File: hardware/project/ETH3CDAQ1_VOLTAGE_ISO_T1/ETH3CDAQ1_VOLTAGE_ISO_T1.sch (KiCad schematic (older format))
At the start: 86 parts, among them J1 GMSTB2,5/2-GF-7,62, J2 Conn_02x10_Odd_Even, U1 DG211, U10 74LVC1GU04DRL, U11 74LVC1GU04DRL, U12 TXB0104PW, U13 24LC08B-E/MS, U14 LT3032-15, U15 PCA9557PW, U2 DG419DY, U3 LT3032, U4 OPA140, U5 ISO124, U6 ADuM5410, U7 DCP020515DU, U8 OPA237_SOT23, U9 74LVC1GU04DRL

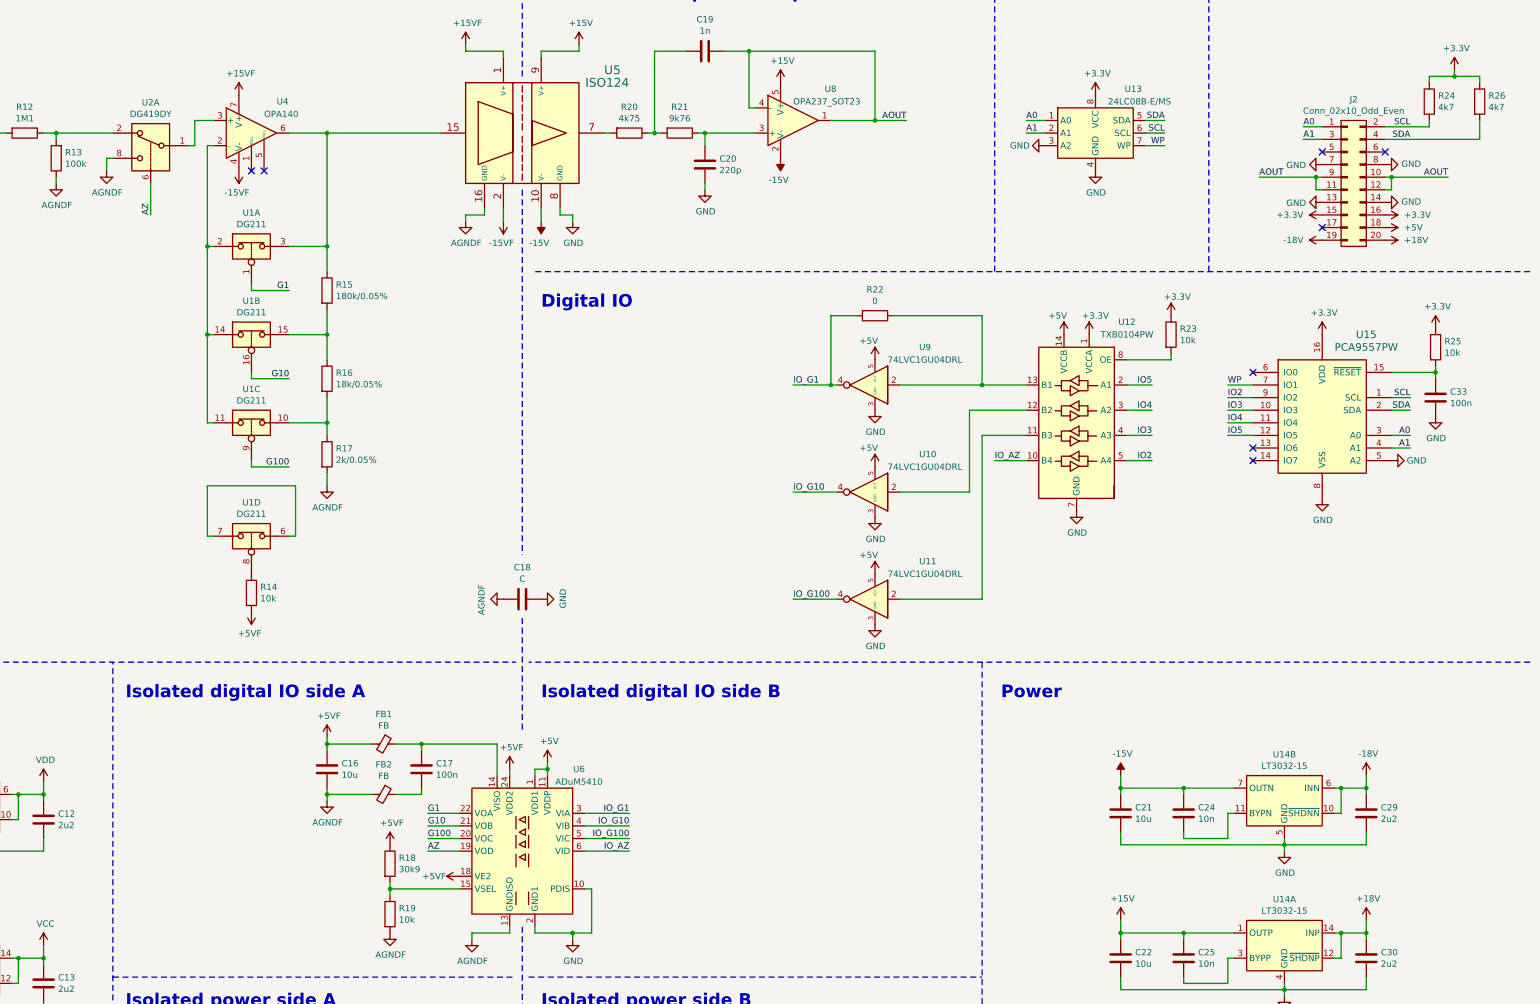
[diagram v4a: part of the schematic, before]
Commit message: Added SDRAM to the linker file.
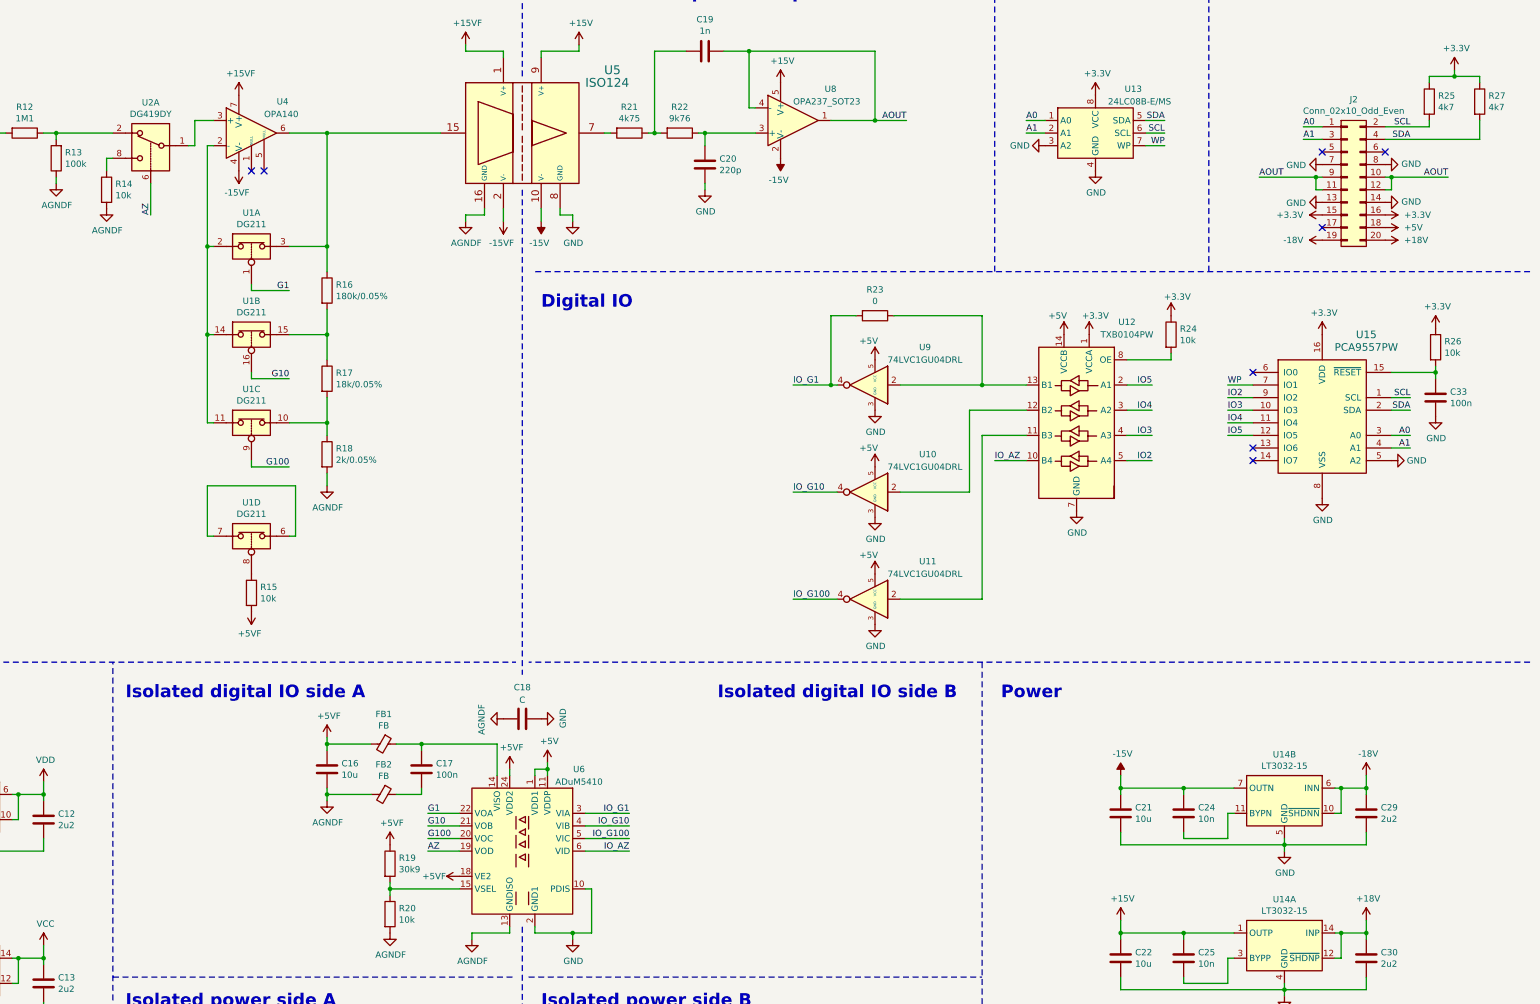
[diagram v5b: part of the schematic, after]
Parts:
- added R14: 10k, Resistor_SMD:R_0603_1608Metric_Pad0.98x0.95mm_HandSolder, symbol Device:R
- renumbered R14 to R15, R15 to R16, R16 to R17, R17 to R18, R18 to R19, R19 to R20, R20 to R21, R21 to R22, R22 to R23, R23 to R24, R24 to R25, R25 to R26, R26 to R27
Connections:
- net AGNDF: now also R14.2; no longer U2.8
- new net: R14.1, U2.8
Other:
- moved on the sheet: C18
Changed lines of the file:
@@
 	5550 2700 5600 2700
 $Comp
-L Device:R R15
+L Device:R R16
 U 1 1 5FCA8528
 P 6500 3050
-F 0 "R15" H 6570 3096 50  0000 L CNN
+F 0 "R16" H 6570 3096 50  0000 L CNN
 F 1 "180k/0.05%" H 6570 3005 50  0000 L CNN
 F 2 "Resistor_SMD:R_0603_1608Metric_Pad0.98x0.95mm_HandSolder" V 6430 3050 50  0001 C CNN
@@
 	5550 3400 5550 2700
 $Comp
-L Device:R R16
+L Device:R R17
 U 1 1 5FCC997F
 P 6500 3750
-F 0 "R16" H 6570 3796 50  0000 L CNN
+F 0 "R17" H 6570 3796 50  0000 L CNN
 F 1 "18k/0.05%" H 6570 3705 50  0000 L CNN
 F 2 "Resistor_SMD:R_0603_1608Metric_Pad0.98x0.95mm_HandSolder" V 6430 3750 50  0001 C CNN
@@
 Connection ~ 5550 3400
 $Comp
-L Device:R R17
+L Device:R R18
 U 1 1 5FCD9876
 P 6500 4350
-F 0 "R17" H 6570 4396 50  0000 L CNN
+F 0 "R18" H 6570 4396 50  0000 L CNN
 F 1 "2k/0.05%" H 6570 4305 50  0000 L CNN
 F 2 "Resistor_SMD:R_0603_1608Metric_Pad0.98x0.95mm_HandSolder" V 6430 4350 50  0001 C CNN
@@
 $EndComp
 $Comp
-L Device:R R14
+L Device:R R15
 U 1 1 5FCE80CD
 P 5900 5450
-F 0 "R14" H 5970 5496 50  0000 L CNN
+F 0 "R15" H 5970 5496 50  0000 L CNN
 F 1 "10k" H 5970 5405 50  0000 L CNN
 F 2 "Resistor_SMD:R_0603_1608Metric_Pad0.98x0.95mm_HandSolder" V 5830 5450 50  0001 C CNN
@@
 L ETH3CDAQ1:AGNDF #PWR028
 U 1 1 5FCEDC4F
-P 4750 2100
-F 0 "#PWR028" H 4750 1850 50  0001 C CNN
-F 1 "AGNDF" H 4755 1927 50  0000 C CNN
-F 2 "" H 4750 2100 50  0001 C CNN
-F 3 "" H 4750 2100 50  0001 C CNN
-	1    4750 2100
+P 4750 2400
+F 0 "#PWR028" H 4750 2150 50  0001 C CNN
+F 1 "AGNDF" H 4755 2227 50  0000 C CNN
+F 2 "" H 4750 2400 50  0001 C CNN
+F 3 "" H 4750 2400 50  0001 C CNN
+	1    4750 2400
 	1    0    0    -1
 $EndComp
@@
 $EndComp
 $Comp
-L Device:R R25
+L Device:R R26
 U 1 1 602F7B40
 P 15300 3500
-F 0 "R25" H 15370 3546 50  0000 L CNN
+F 0 "R26" H 15370 3546 50  0000 L CNN
 F 1 "10k" H 15370 3455 50  0000 L CNN
 F 2 "Resistor_SMD:R_0603_1608Metric_Pad0.98x0.95mm_HandSolder" V 15230 3500 50  0001 C CNN
@@
 $EndComp
 $Comp
-L Device:R R20
+L Device:R R21
 U 1 1 60139864
 P 8900 1800
-F 0 "R20" V 8693 1800 50  0000 C CNN
+F 0 "R21" V 8693 1800 50  0000 C CNN
 F 1 "4k75" V 8784 1800 50  0000 C CNN
 F 2 "Resistor_SMD:R_0603_1608Metric_Pad0.98x0.95mm_HandSolder" V 8830 1800 50  0001 C CNN
@@
 $EndComp
 $Comp
-L Device:R R21
+L Device:R R22
 U 1 1 60164665
 P 9300 1800
-F 0 "R21" V 9093 1800 50  0000 C CNN
+F 0 "R22" V 9093 1800 50  0000 C CNN
 F 1 "9k76" V 9184 1800 50  0000 C CNN
 F 2 "Resistor_SMD:R_0603_1608Metric_Pad0.98x0.95mm_HandSolder" V 9230 1800 50  0001 C CNN
@@
 	7950 6850 7950 6900
 $Comp
-L Device:R R18
+L Device:R R19
 U 1 1 60785009
 P 7000 7600
-F 0 "R18" H 7070 7646 50  0000 L CNN
+F 0 "R19" H 7070 7646 50  0000 L CNN
 F 1 "30k9" H 7070 7555 50  0000 L CNN
 F 2 "Resistor_SMD:R_0603_1608Metric_Pad0.98x0.95mm_HandSolder" V 6930 7600 50  0001 C CNN
@@
 $EndComp
 $Comp
-L Device:R R19
+L Device:R R20
 U 1 1 60785EBE
 P 7000 8000
-F 0 "R19" H 7070 8046 50  0000 L CNN
+F 0 "R20" H 7070 8046 50  0000 L CNN
 F 1 "10k" H 7070 7955 50  0000 L CNN
 F 2 "Resistor_SMD:R_0603_1608Metric_Pad0.98x0.95mm_HandSolder" V 6930 8000 50  0001 C CNN
@@
 $EndComp
 $Comp
-L Device:R R24
+L Device:R R25
 U 1 1 618DCF7E
 P 15250 1550
-F 0 "R24" H 15320 1596 50  0000 L CNN
+F 0 "R25" H 15320 1596 50  0000 L CNN
 F 1 "4k7" H 15320 1505 50  0000 L CNN
 F 2 "Resistor_SMD:R_0603_1608Metric_Pad0.98x0.95mm_HandSolder" V 15180 1550 50  0001 C CNN
@@
 $EndComp
 $Comp
-L Device:R R26
+L Device:R R27
 U 1 1 618DE37E
 P 15650 1550
-F 0 "R26" H 15720 1596 50  0000 L CNN
+F 0 "R27" H 15720 1596 50  0000 L CNN
 F 1 "4k7" H 15720 1505 50  0000 L CNN
 F 2 "Resistor_SMD:R_0603_1608Metric_Pad0.98x0.95mm_HandSolder" V 15580 1550 50  0001 C CNN
@@
 IO5
 $Comp
-L Device:R R23
+L Device:R R24
 U 1 1 600D6137
 P 13200 3400
-F 0 "R23" H 13270 3446 50  0000 L CNN
+F 0 "R24" H 13270 3446 50  0000 L CNN
 F 1 "10k" H 13270 3355 50  0000 L CNN
 F 2 "Resistor_SMD:R_0603_1608Metric_Pad0.98x0.95mm_HandSolder" V 13130 3400 50  0001 C CNN
@@
 $EndComp
 $Comp
-L Device:R R22
+L Device:R R23
 U 1 1 602E40CD
 P 10850 3250
-F 0 "R22" V 10643 3250 50  0000 C CNN
+F 0 "R23" V 10643 3250 50  0000 C CNN
 F 1 "0" V 10734 3250 50  0000 C CNN
 F 2 "Resistor_SMD:R_0603_1608Metric_Pad0.98x0.95mm_HandSolder" V 10780 3250 50  0001 C CNN
@@
 	11700 3800 12050 3800
 Wire Notes Line width 20 rgb(255, 0, 0)
-	8050 2250 8050 5150
+	8050 2250 8050 6100
 Wire Notes Line width 20 rgb(255, 0, 0)
 	8050 8100 8050 9000
@@
 L Device:C C18
 U 1 1 5FD914EF
-P 8050 5500
-F 0 "C18" V 7798 5500 50  0000 C CNN
-F 1 "C" V 7889 5500 50  0000 C CNN
-F 2 "Capacitor_SMD:C_1812_4532Metric_Pad1.57x3.40mm_HandSolder" H 8088 5350 50  0001 C CNN
-F 3 "~" H 8050 5500 50  0001 C CNN
-	1    8050 5500
+P 8050 6450
+F 0 "C18" V 7800 6450 50  0000 C CNN
+F 1 "C" V 7900 6450 50  0000 C CNN
+F 2 "Capacitor_SMD:C_1812_4532Metric_Pad1.57x3.40mm_HandSolder" H 8088 6300 50  0001 C CNN
+F 3 "~" H 8050 6450 50  0001 C CNN
+	1    8050 6450
 	0    1    1    0
 $EndComp
-Wire Notes Line width 20 rgb(255, 0, 0)
-	8050 5650 8050 6550
 $Comp
 L ETH3CDAQ1:AGNDF #PWR049
 U 1 1 5FE93A9B
-P 7900 5500
-F 0 "#PWR049" H 7900 5250 50  0001 C CNN
-F 1 "AGNDF" H 7905 5327 50  0000 C CNN
-F 2 "" H 7900 5500 50  0001 C CNN
-F 3 "" H 7900 5500 50  0001 C CNN
-	1    7900 5500
+P 7900 6450
+F 0 "#PWR049" H 7900 6200 50  0001 C CNN
+F 1 "AGNDF" H 7905 6277 50  0000 C CNN
+F 2 "" H 7900 6450 50  0001 C CNN
+F 3 "" H 7900 6450 50  0001 C CNN
+	1    7900 6450
 	0    1    1    0
 $EndComp
@@
 L power:GND #PWR052
 U 1 1 5FE966AE
-P 8200 5500
-F 0 "#PWR052" H 8200 5250 50  0001 C CNN
-F 1 "GND" H 8205 5327 50  0000 C CNN
-F 2 "" H 8200 5500 50  0001 C CNN
-F 3 "" H 8200 5500 50  0001 C CNN
-	1    8200 5500
+P 8200 6450
+F 0 "#PWR052" H 8200 6200 50  0001 C CNN
+F 1 "GND" H 8205 6277 50  0000 C CNN
+F 2 "" H 8200 6450 50  0001 C CNN
+F 3 "" H 8200 6450 50  0001 C CNN
+	1    8200 6450
 	0    -1   -1   0
 $EndComp
@@
 	0    1    1    0
 $EndComp
-Text Notes 8200 6300 0    100  ~ 20
+Text Notes 9600 6300 0    100  ~ 20
 Isolated digital IO side B
 Text Notes 4900 6300 0    100  ~ 20
@@
 Wire Wire Line
 	7250 6650 7850 6650
+$Comp
+L Device:R R14
+U 1 1 5FF45F8E
+P 4750 2250
+F 0 "R14" H 4820 2296 50  0000 L CNN
+F 1 "10k" H 4820 2205 50  0000 L CNN
+F 2 "Resistor_SMD:R_0603_1608Metric_Pad0.98x0.95mm_HandSolder" V 4680 2250 50  0001 C CNN
+F 3 "~" H 4750 2250 50  0001 C CNN
+	1    4750 2250
+	1    0    0    -1
+$EndComp
 $EndSCHEMATC
